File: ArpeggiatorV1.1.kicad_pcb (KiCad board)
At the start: 2 copper layers, 0 parts

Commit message: Adjusted pin assigments for a cleaner layout. Partially laid out and routed board.
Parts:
- added C1: 0.1u, Capacitor_THT:C_Disc_D3.0mm_W1.6mm_P2.50mm, F.Cu at (36.6, -49.9)
- added C2: 0.1u, Capacitor_THT:C_Disc_D3.0mm_W1.6mm_P2.50mm, F.Cu at (34.1, -46.7)
- added C3: 0.1u, Capacitor_THT:C_Disc_D3.0mm_W1.6mm_P2.50mm, F.Cu at (36.6, -43.6)
- added C4: 0.1u, Capacitor_THT:C_Disc_D3.0mm_W1.6mm_P2.50mm, F.Cu at (36.6, -40.4)
- added C5: 1u, Capacitor_THT:C_Disc_D3.0mm_W1.6mm_P2.50mm, F.Cu at (-8.23, 55.8)
- added C6: 1u, Capacitor_THT:C_Disc_D3.0mm_W1.6mm_P2.50mm, F.Cu at (-5.08, 53.3)
- added C7: 10u, Capacitor_THT:CP_Radial_D5.0mm_P2.50mm, F.Cu at (154.9, 40.6)
- added D1: 1N914, Diode_THT:D_A-405_P7.62mm_Horizontal, F.Cu at (30.1, -30.2)
- added D10: LED, LED_THT:LED_D3.0mm, F.Cu at (62.2, 110.5)
- added D11: LED, LED_THT:LED_D3.0mm, F.Cu at (62.2, 104.1)
- added D12: LED, LED_THT:LED_D3.0mm, F.Cu at (62.2, 97.8)
- added D13: LED, LED_THT:LED_D3.0mm, F.Cu at (62.2, 91.4)
- added D14: LED, LED_THT:LED_D3.0mm, F.Cu at (109.2, 116.8)
- added D15: LED, LED_THT:LED_D3.0mm, F.Cu at (129.5, 116.8)
- added D16: LED, LED_THT:LED_D3.0mm, F.Cu at (129.5, 106.7)
- added D2: 1N914, Diode_THT:D_A-405_P7.62mm_Horizontal, F.Cu at (30.1, -25.9)
- added D3: LED, LED_THT:LED_D3.0mm, F.Cu at (43.2, 106.7)
- added D4: LED, LED_THT:LED_D3.0mm, F.Cu at (43.2, 116.8)
- added D5: LED, LED_THT:LED_D3.0mm, F.Cu at (80.0, 97.8)
- added D6: LED, LED_THT:LED_D3.0mm, F.Cu at (80.0, 104.1)
- added D7: LED, LED_THT:LED_D3.0mm, F.Cu at (80.0, 110.5)
- added D8: LED, LED_THT:LED_D3.0mm, F.Cu at (80.0, 116.8)
- added D9: LED, LED_THT:LED_D3.0mm, F.Cu at (62.2, 116.8)
- added H1: MountingHole, MountingHole:MountingHole_4mm, F.Cu at (40.6, 64.8)
- added H2: MountingHole, MountingHole:MountingHole_4mm, F.Cu at (129.5, 40.6)
- added H3: MountingHole, MountingHole:MountingHole_4mm, F.Cu at (119.4, 128.3)
- added H4: MountingHole, MountingHole:MountingHole_4mm, F.Cu at (53.3, 128.3)
- added H5: MountingHole, MountingHole:MountingHole_4mm, F.Cu at (92.7, 128.3)
- added H6: MountingHole, MountingHole:MountingHole_4mm, F.Cu at (102.9, 40.6)
- added J1: DIN-5_MIDI_IN, Eurocad:MIDI_DIN5, B.Cu at (47.0, 44.5)
- added J2: DIN-5_SYNC_IN, Eurocad:MIDI_DIN5, B.Cu at (67.3, 44.5)
- added J3: DIN-5_MIDI_OUT, Eurocad:MIDI_DIN5, B.Cu at (87.6, 44.5)
- added J4: Conn_01x03_Pin, Connector_PinHeader_2.54mm:PinHeader_1x03_P2.54mm_Horizontal, B.Cu at (118.1, 45.0)
- added R1: 220, Resistor_THT:R_Axial_DIN0207_L6.3mm_D2.5mm_P10.16mm_Horizontal, F.Cu at (22.8, -67.2)
- added R10: 220, Resistor_THT:R_Axial_DIN0207_L6.3mm_D2.5mm_P10.16mm_Horizontal, F.Cu at (86.4, 119.4)
- added R11: 220, Resistor_THT:R_Axial_DIN0207_L6.3mm_D2.5mm_P10.16mm_Horizontal, F.Cu at (71.1, 119.4)
- added R12: 4k7, Resistor_THT:R_Axial_DIN0207_L6.3mm_D2.5mm_P10.16mm_Horizontal, F.Cu at (35.0, -57.1)
- added R13: 4k7, Resistor_THT:R_Axial_DIN0207_L6.3mm_D2.5mm_P10.16mm_Horizontal, F.Cu at (39.0, -57.1)
- added R14: 470, Resistor_THT:R_Axial_DIN0207_L6.3mm_D2.5mm_P10.16mm_Horizontal, F.Cu at (43.1, -67.2)
- added R15: 470, Resistor_THT:R_Axial_DIN0207_L6.3mm_D2.5mm_P10.16mm_Horizontal, F.Cu at (47.1, -57.1)
- added R16: 220, Resistor_THT:R_Axial_DIN0207_L6.3mm_D2.5mm_P10.16mm_Horizontal, F.Cu at (67.3, 119.4)
- added R17: 220, Resistor_THT:R_Axial_DIN0207_L6.3mm_D2.5mm_P10.16mm_Horizontal, F.Cu at (71.1, 104.1)
- added R18: 220, Resistor_THT:R_Axial_DIN0207_L6.3mm_D2.5mm_P10.16mm_Horizontal, F.Cu at (67.3, 104.1)
- added R19: 220, Resistor_THT:R_Axial_DIN0207_L6.3mm_D2.5mm_P10.16mm_Horizontal, F.Cu at (57.1, 106.7)
- added R2: 220, Resistor_THT:R_Axial_DIN0207_L6.3mm_D2.5mm_P10.16mm_Horizontal, F.Cu at (34.1, -53.5)
- added R20: 220, Resistor_THT:R_Axial_DIN0207_L6.3mm_D2.5mm_P10.16mm_Horizontal, F.Cu at (115.6, 119.4)
- added R21: 220, Resistor_THT:R_Axial_DIN0207_L6.3mm_D2.5mm_P10.16mm_Horizontal, F.Cu at (119.4, 119.4)
- added R22: 220, Resistor_THT:R_Axial_DIN0207_L6.3mm_D2.5mm_P10.16mm_Horizontal, F.Cu at (123.2, 119.4)
- added R23: 15k, Resistor_THT:R_Axial_DIN0207_L6.3mm_D2.5mm_P10.16mm_Horizontal, F.Cu at (-15.9, 43.6)
- added R24: 15k, Resistor_THT:R_Axial_DIN0207_L6.3mm_D2.5mm_P10.16mm_Horizontal, F.Cu at (-11.8, 53.8)
- added R3: 10, Resistor_THT:R_Axial_DIN0207_L6.3mm_D2.5mm_P10.16mm_Horizontal, F.Cu at (26.9, -67.2)
- added R4: 33, Resistor_THT:R_Axial_DIN0207_L6.3mm_D2.5mm_P10.16mm_Horizontal, F.Cu at (30.9, -67.2)
- added R5: 220, Resistor_THT:R_Axial_DIN0207_L6.3mm_D2.5mm_P10.16mm_Horizontal, F.Cu at (48.3, 116.8)
- added R6: 220, Resistor_THT:R_Axial_DIN0207_L6.3mm_D2.5mm_P10.16mm_Horizontal, F.Cu at (52.1, 116.8)
- added R7: 220, Resistor_THT:R_Axial_DIN0207_L6.3mm_D2.5mm_P10.16mm_Horizontal, F.Cu at (86.4, 108.0)
- added R8: 220, Resistor_THT:R_Axial_DIN0207_L6.3mm_D2.5mm_P10.16mm_Horizontal, F.Cu at (86.4, 111.8)
- added R9: 220, Resistor_THT:R_Axial_DIN0207_L6.3mm_D2.5mm_P10.16mm_Horizontal, F.Cu at (86.4, 115.6)
- added RV1: 10k (B), Connector_PinHeader_2.54mm:PinHeader_1x03_P2.54mm_Vertical, F.Cu at (-7.48, 44.4)
- added RV2: 10k (B), Connector_PinHeader_2.54mm:PinHeader_1x03_P2.54mm_Vertical, F.Cu at (-2.83, 44.4)
- added SW1: SW_SYNC, Button_Switch_THT:SW_PUSH_6mm, F.Cu at (46.4, 130.5)
- added SW2: SW_MODE, Button_Switch_THT:SW_PUSH_6mm, F.Cu at (85.8, 130.5)
- added SW3: SW_OCT, Button_Switch_THT:SW_PUSH_6mm, F.Cu at (68.0, 130.5)
- added SW4: SW_ONOFF, Button_Switch_THT:SW_PUSH_6mm, F.Cu at (112.5, 130.5)
- added SW5: SW_HOLD, Button_Switch_THT:SW_PUSH_6mm, F.Cu at (132.8, 130.5)
- added U1: 6N138, Package_DIP:DIP-8_W7.62mm_LongPads, F.Cu at (30.5, -53.5)
- added U2: 6N138, Package_DIP:DIP-8_W7.62mm_LongPads, F.Cu at (30.5, -41.9)
- added U3: Pico, MCU_RaspberryPi_and_Boards:RPi_Pico_SMD_TH, B.Cu at (109.2, 80.0)
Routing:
- net /SYNC: track 0.00 -> 112.3 mm
- net /OCT5_LED: track 0.00 -> 80.2 mm
- net GND: track 0.00 -> 80.0 mm
- net /TEMPO_LED: track 0.00 -> 79.5 mm
- net /SYNC_LED: track 0.00 -> 74.9 mm
- net /OCT: track 0.00 -> 59.3 mm
- net /MODE: track 0.00 -> 58.4 mm
- net /HOLD: track 0.00 -> 47.3 mm
- net /OCT2_LED: track 0.00 -> 47.0 mm
- net /ONOFF: track 0.00 -> 46.0 mm
- net /OCT4_LED: track 0.00 -> 43.8 mm
- net /OCT3_LED: track 0.00 -> 35.5 mm
- net /MODE_RANDOM_LED: track 0.00 -> 32.1 mm
- net /OCT1_LED: track 0.00 -> 29.1 mm
- net /MODE_UP_DOWN_LED: track 0.00 -> 27.6 mm
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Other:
- board outline added: 100 x 100 mm

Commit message: Mostly finished PCB layout.
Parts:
- moved R3 157.2 mm to (132.1, 49.5)
- moved R4 152.0 mm to (128.3, 49.5)
- moved R14 148.6 mm to (47.6, 81.3), turned to 0 degrees
- moved R15 142.4 mm to (71.8, 83.2), turned to 180 degrees
- moved R1 134.6 mm to (57.1, 62.9), turned to 180 degrees
- moved R12 128.5 mm to (43.8, 71.1), turned to -90 degrees
- moved R13 125.3 mm to (79.4, 61.6), turned to 0 degrees
- moved C4 125.3 mm to (71.1, 80.0)
- moved U1 124.7 mm to (55.8, 68.6)
- moved C3 122.5 mm to (59.1, 76.8), turned to 90 degrees
- moved C5 121.7 mm to (113.0, 66.0), turned to 0 degrees
- moved R2 120.1 mm to (64.1, 62.9)
- moved C6 118.5 mm to (113.0, 63.5), turned to 0 degrees
- moved U2 117.7 mm to (71.1, 68.6)
- moved C2 109.8 mm to (63.5, 59.0), turned to 90 degrees
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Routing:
- net /MIDI_IN: track 0.00 -> 148.2 mm
- net GNDA: track 0.00 -> 133.3 mm
- net /MIDI_SYNC_IN: track 0.00 -> 123.8 mm
- net /TEMPO: track 0.00 -> 93.9 mm, vias 0 -> 2
- net /GATE: track 0.00 -> 91.9 mm, vias 0 -> 2
- net Net-(J4-Pin_1): track 0.00 -> 65.8 mm, vias 0 -> 1
- net Net-(J4-Pin_3): track 0.00 -> 62.4 mm, vias 0 -> 2
- net Net-(J3-Pad5): track 0.00 -> 55.9 mm
- net GND: track 80.0 -> 40.8 mm
- net Net-(J3-Pad4): track 0.00 -> 36.9 mm
- net Net-(D1-A): track 0.00 -> 35.8 mm
- net /MIDI_OUT: track 0.00 -> 32.9 mm
- net Net-(C2-Pad1): track 0.00 -> 28.8 mm
- net Net-(D2-A): track 0.00 -> 24.6 mm
- net VCC: track 0.00 -> 20.4 mm
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
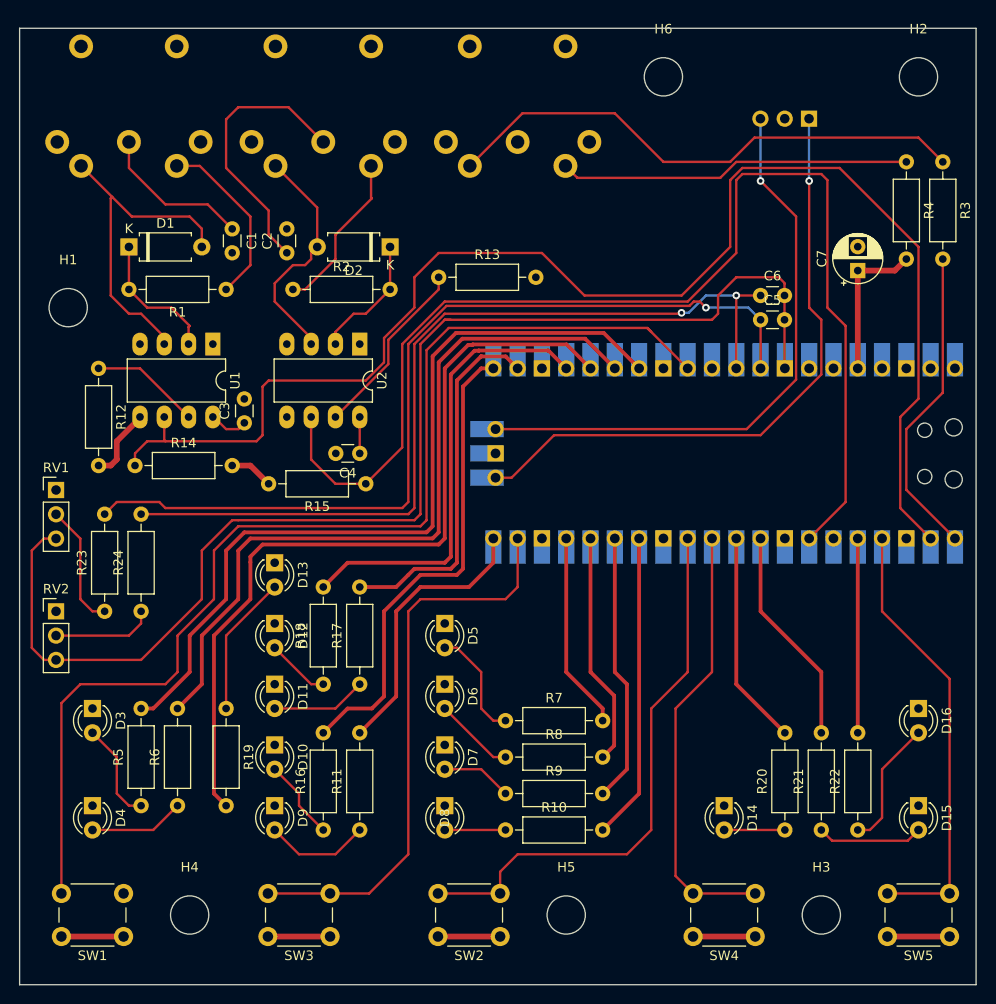
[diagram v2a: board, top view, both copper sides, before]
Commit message: Finished routing missing signals.
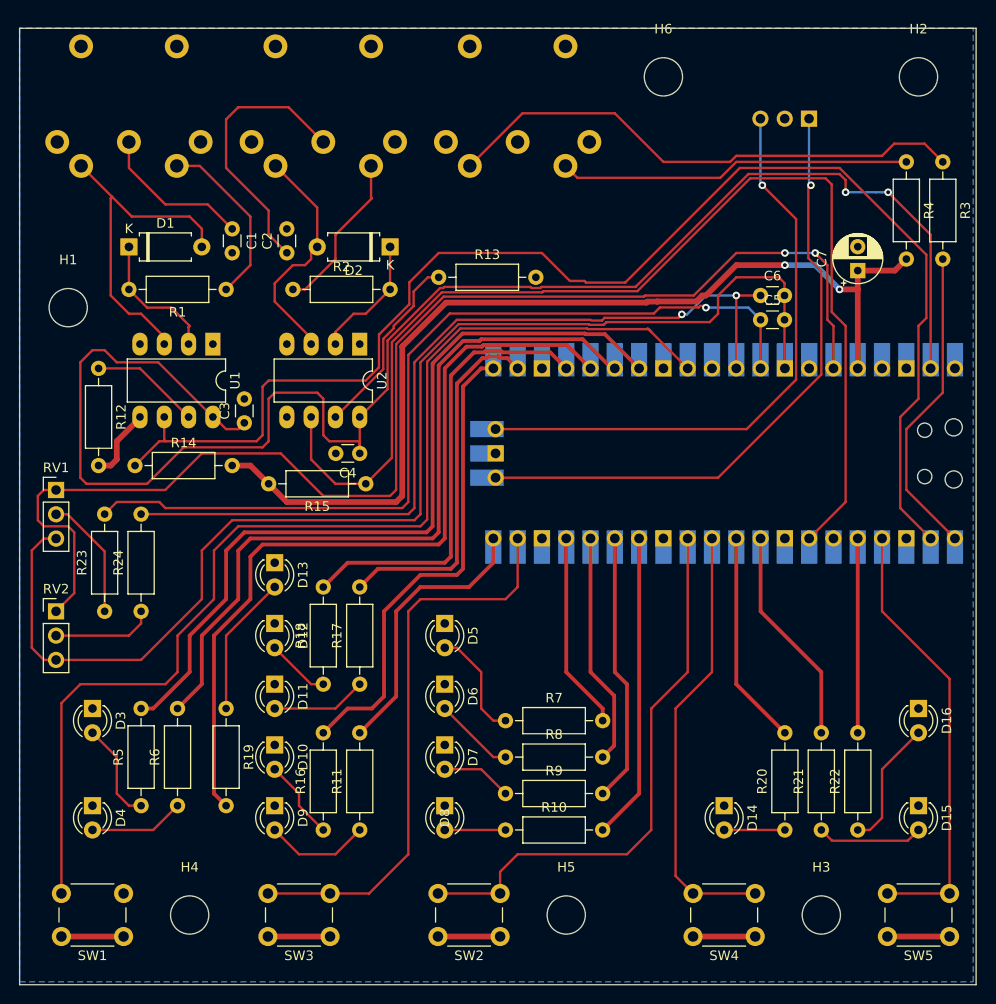
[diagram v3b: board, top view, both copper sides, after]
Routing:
- net +5V: track 7.91 -> 168.9 mm, vias 0 -> 2
- net /ADC_VREF: track 0.00 -> 133.2 mm, vias 0 -> 2
- net VCC: track 20.4 -> 103.3 mm, vias 0 -> 2
- net /MIDI_IN: track 148.2 -> 143.0 mm
- net /MIDI_SYNC_IN: track 123.8 -> 119.7 mm
- net GNDA: track 133.3 -> 131.6 mm
- net /GATE: track 91.9 -> 90.7 mm
- net /TEMPO: track 93.9 -> 92.8 mm
- net /SYNC: track 119.5 -> 118.8 mm
- net Net-(U2-VO1): track 19.1 -> 19.7 mm
- net Net-(J3-Pad5): track 55.9 -> 55.4 mm
- added copper zone on B.Cu, net GND

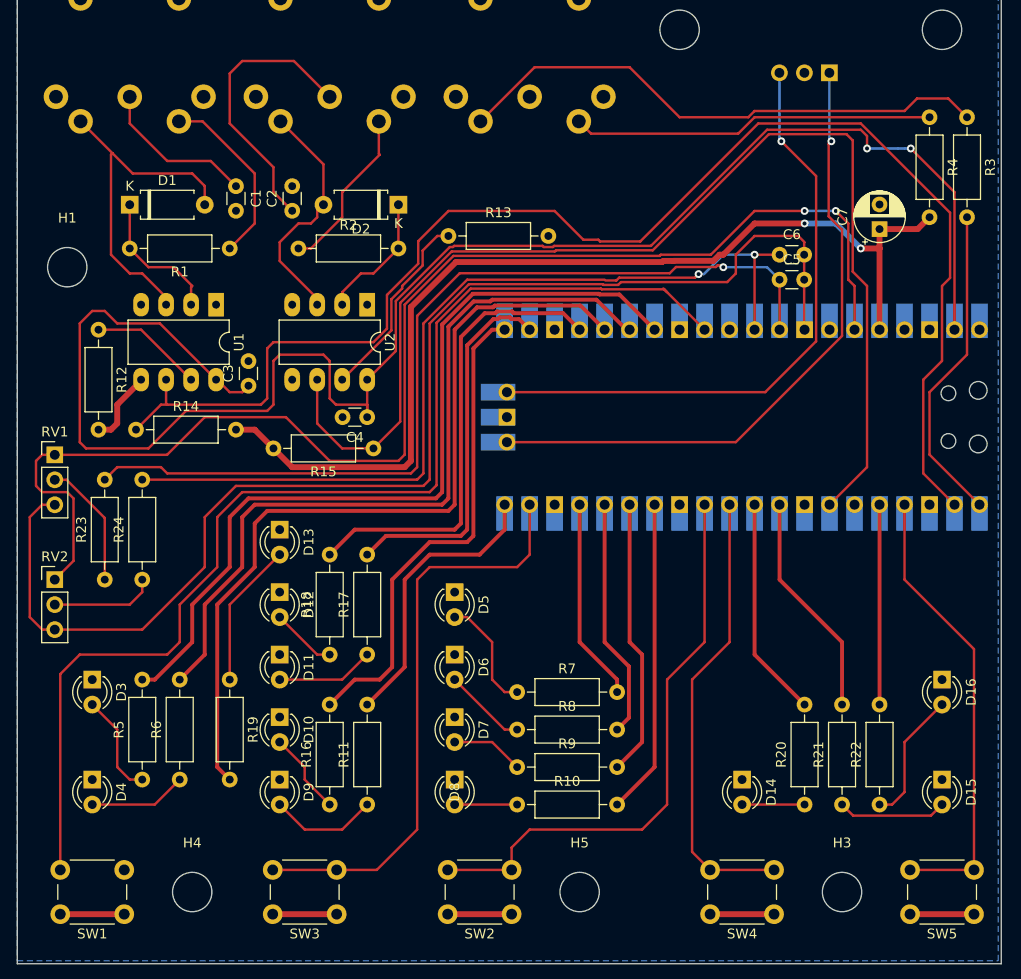
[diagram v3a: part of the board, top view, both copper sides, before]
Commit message: Cleaned up PCB and fixed some DRC warnings.
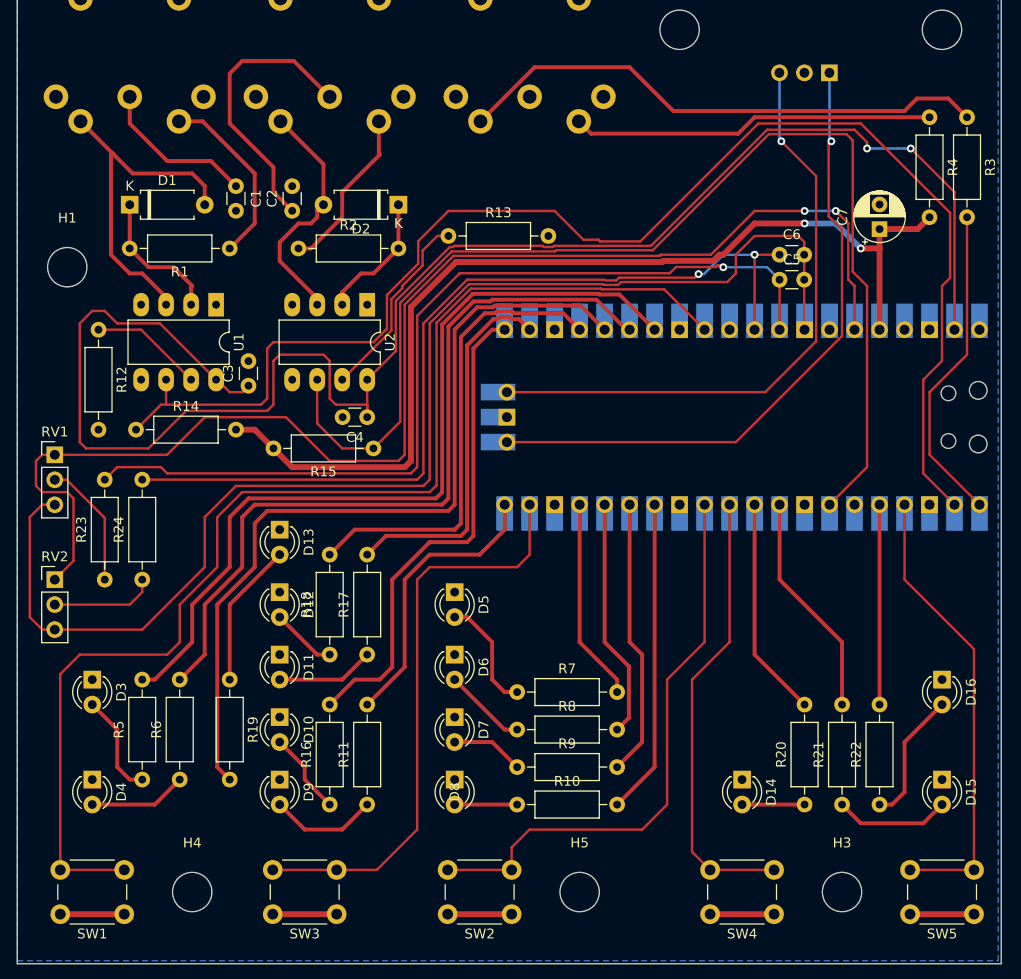
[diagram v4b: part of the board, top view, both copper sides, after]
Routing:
- net GND: track 40.8 -> 32.8 mm
- net /SYNC: track 118.8 -> 124.7 mm
- net /HOLD: track 47.3 -> 46.5 mm
- net Net-(D15-A): track 11.1 -> 11.7 mm
- net Net-(J3-Pad5): track 55.4 -> 54.9 mm

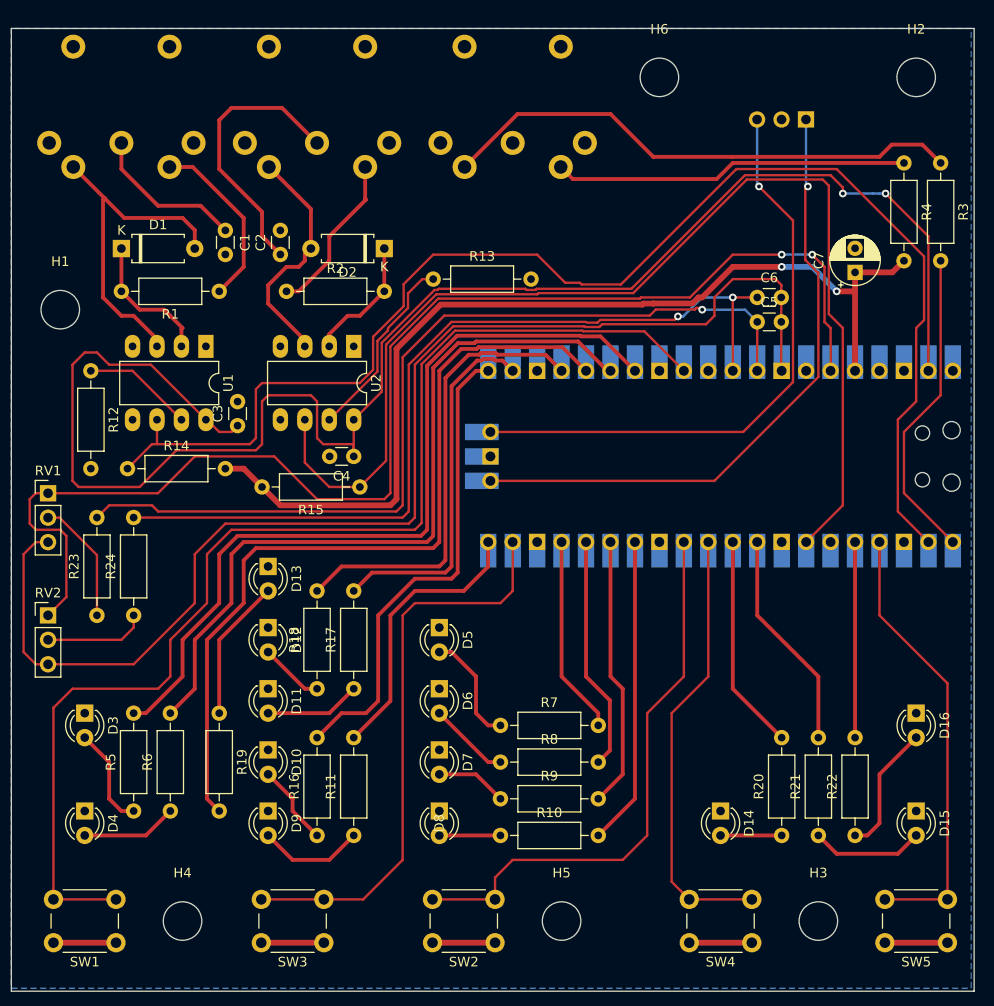
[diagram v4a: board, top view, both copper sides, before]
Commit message: Fixed minor PCB issues.
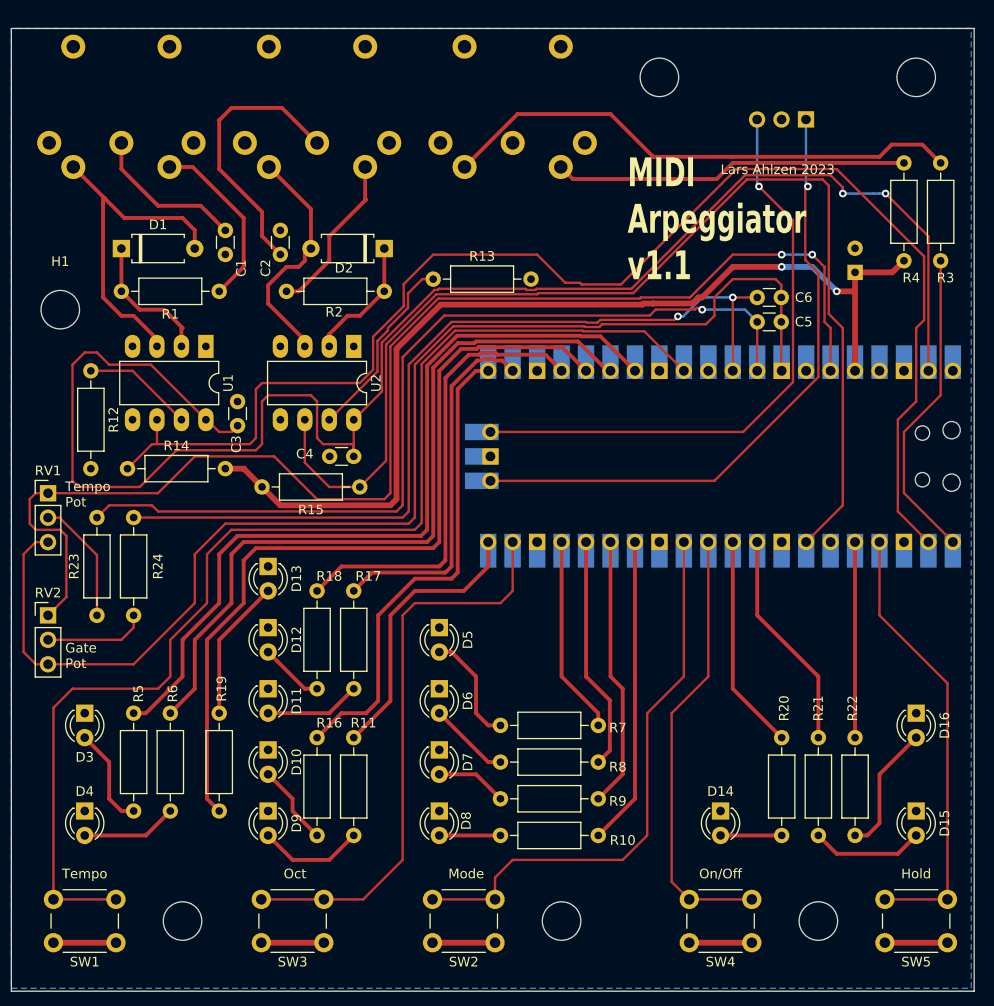
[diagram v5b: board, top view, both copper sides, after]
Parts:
- C7: moved to B.Cu
- J1: value DIN-5_MIDI_IN -> DIN-5 MIDI_IN
- J2: value DIN-5_SYNC_IN -> DIN-5 SYNC_IN
- J3: value DIN-5_MIDI_OUT -> DIN-5 MIDI_OUT
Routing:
- net Net-(J4-Pin_3): vias 2 -> 1
- net /TEMPO: vias 2 -> 1
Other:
- board text added: "Gate Pot"
- board text added: "Hold"
- board text added: "Lars Ahlzen 2023"
- board text added: "MIDI Arpeggiator v1.1"
- board text added: "Mode"
- board text added: "Oct"
- board text added: "On/Off"
- board text added: "Raspberry Pi Pico"
- board text added: "Tempo"
- board text added: "Tempo Pot"

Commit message: More minor PCB adjustments.
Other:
- board text added: "Serial:"
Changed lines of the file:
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@@
     (property "ki_keywords" "mounting hole")
     (attr exclude_from_pos_files)
-    (fp_text reference "H1" (at 0 -5) (layer "F.SilkS")
+    (fp_text reference "H1" (at 0 -5) (layer "F.SilkS") hide
         (effects (font (size 1 1) (thickness 0.15)))
     )
@@
     )
   )
+  (gr_rect (start 103.124 74.676) (end 127 80.264)
+    (stroke (width 0.15) (type solid)) (fill solid) (layer "F.SilkS"))
   (gr_rect (start 35.56 35.56) (end 135.56 135.56)
     (stroke (width 0.1) (type default)) (fill none) (layer "Edge.Cuts"))
@@
     (effects (font (size 3 2) (thickness 0.4) bold) (justify left bottom))
   )
+  (gr_text "Serial:" (at 91.948 79.248) (layer "F.SilkS")
+    (effects (font (size 2 2) (thickness 0.15)) (justify left bottom))
+  )
   (gr_text "Hold" (at 129.54 123.952) (layer "F.SilkS")
